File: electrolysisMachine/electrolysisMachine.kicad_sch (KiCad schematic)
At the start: 1 part

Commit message: started work on shcematic
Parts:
- added C?: 100n, Capacitor_SMD:C_0805_2012Metric_Pad1.18x1.45mm_HandSolder, symbol 000_Capacitor_FIlm_Immo:cap_film_0805
- added R?: 260r, Resistor_SMD:R_0805_2012Metric_Pad1.20x1.40mm_HandSolder, symbol 000_Resistors_Immo:Resistor_0805
- added SW?: Power, symbol Switch:SW_SPST
- added U?: LM317_SOT-223, Package_TO_SOT_THT:TO-220-3_Vertical, symbol Regulator_Linear:LM317_SOT-223
- added U?: LM317_TO-220, Package_SO:SOIC-8_3.9x4.9mm_P1.27mm, symbol Regulator_Linear:LM317_TO-220
- added Vtrim: 5k, Potentiometer_THT:Potentiometer_Alps_RK09K_Single_Vertical, symbol Device:R_Potentiometer_Trim
- J?: value XT60_connector_DC_60A_male -> XT60_60A_m
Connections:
- net 30V_BUS: now also C?.1, SW?.2 (B), U?.3 (VI), U?.3 (VI); no longer J?.2 (V+)
- net GNDPWR: now also C?.2, Vtrim.1
- new net: R?.2, U?.1 (ADJ), U?.1 (ADJ), Vtrim.2, Vtrim.3
- new net: J?.2 (V+), SW?.1 (A)
- new net V_ANODE: R?.1, U?.2 (VO), U?.2 (VO)
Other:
- note added: "Or use charge Pump?"

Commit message: nhj
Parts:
- added C? (x2): 1u, Capacitor_SMD:CP_Elec_6.3x5.9, symbol 000_Capacitor_Electrolytic_Immo:22u
- added C?: 100n, Capacitor_SMD:C_0805_2012Metric_Pad1.18x1.45mm_HandSolder, symbol 000_Capacitor_FIlm_Immo:cap_film_0805
- added D?: LED_0805_smd, Diode_SMD:D_0805_2012Metric_Pad1.15x1.40mm_HandSolder, symbol 000_Diodes_Immo:LED_0805_smd
- added R?: 260r, Resistor_SMD:R_0805_2012Metric_Pad1.20x1.40mm_HandSolder, symbol 000_Resistors_Immo:Resistor_0805
- added U?: L7805, Package_TO_SOT_THT:TO-220F-3_Horizontal_TabDown, symbol Regulator_Linear:L7805
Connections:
- net GNDPWR: now also C?.2, C?.2, C?.2, R?.2, U?.2 (GND)
- net V_ANODE: now also C?.1, C?.1, U?.1 (IN)
- new net: D?.1 (K), R?.1
- new net 5V_BUS: C?.1, D?.2 (A), U?.3 (OUT)

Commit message: Schematic Layout Continued
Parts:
- added J?: Anode/Cathode, symbol 000_Connectors_Immo:XT60_connector_DC_30A_female
- added Q?: PN2222A, Package_TO_SOT_SMD:SOT-223-3_TabPin2, symbol Transistor_BJT:PN2222A
- added R?: 1k, Resistor_SMD:R_0805_2012Metric_Pad1.20x1.40mm_HandSolder, symbol 000_Resistors_Immo:Resistor_0805
- added SW?: SW_SPST, symbol Switch:SW_SPST
- added TP?: A_meter, symbol Connector:TestPoint_2Pole
- added TP?: V_meter, symbol Connector:TestPoint_2Pole
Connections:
- net GNDPWR: now also R?.2, TP?.1
- net V_ANODE: now also J?.2 (V+), SW?.1 (A), TP?.2
- new net: Q?.1 (E), R?.1
- new net: Q?.3 (C), TP?.1
- new net: J?.1 (V-), SW?.2 (B), TP?.2

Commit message: schem
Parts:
- added C?: cap_film_0805, Capacitor_SMD:C_0805_2012Metric_Pad1.18x1.45mm_HandSolder, symbol 000_Capacitor_FIlm_Immo:cap_film_0805
- added D?: LED_ORANGE, Diode_SMD:D_0805_2012Metric_Pad1.15x1.40mm_HandSolder, symbol 000_Diodes_Immo:LED_0805_smd
- added Q?: 2N3906, Package_TO_SOT_THT:TO-92_Inline, symbol Transistor_BJT:2N3906
- added R: 1k2, Resistor_SMD:R_0805_2012Metric_Pad1.20x1.40mm_HandSolder, symbol 000_Resistors_Immo:Resistor_0805
- added R? (x2): 12k, Resistor_SMD:R_0805_2012Metric_Pad1.20x1.40mm_HandSolder, symbol 000_Resistors_Immo:Resistor_0805
- added R?: 2k9, Resistor_SMD:R_0805_2012Metric_Pad1.20x1.40mm_HandSolder, symbol 000_Resistors_Immo:Resistor_0805
- added R? (x3): 15k, Resistor_SMD:R_0805_2012Metric_Pad1.20x1.40mm_HandSolder, symbol 000_Resistors_Immo:Resistor_0805
- added R?: 2k2, Resistor_SMD:R_0805_2012Metric_Pad1.20x1.40mm_HandSolder, symbol 000_Resistors_Immo:Resistor_0805
- added RV?: Current, Potentiometer_THT:Potentiometer_Alpha_RD901F-40-00D_Single_Vertical, symbol Device:R_Potentiometer
- added U? (x5): LM324, symbol Amplifier_Operational:LM324
- D?: value LED_0805_smd -> LED_BLUE
- SW?: value SW_SPST -> TestLoad
- renumbered Vtrim to Voltage
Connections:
- net 5V_BUS: now also C?.1, R?.1, R?.2, R?.2, U?.12 (+), U?.4 (V+)
- net GNDPWR: now also C?.2, R.1, R?.1, R?.2, RV?.1, U?.11 (V-)
- net at Q?.1 (E), R?.1: now also U?.2 (-)
- net at Q?.2 (B): now also U?.1
- new net: U?.13 (-), U?.14
- new net: RV?.2, U?.3 (+)
- new net: R?.1, R?.2, U?.5 (+)
- new net: D?.1 (K), R.2
- new net: R?.1, R?.1, U?.7
- new net: Q?.2 (B), R?.2
- new net: R?.1, R?.2, U?.9 (-)
- new net: D?.2 (A), R?.2, U?.8
- new net: Q?.1 (E), R?.1
- new net: Q?.3 (C), RV?.3
- new net TRIGGER: U?.10 (+), U?.6 (-)
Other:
- note added: "Transistor Orientation Unclear"
- moved on the sheet: C?, D?, J?, Q?, R?, SW?, TP?, U?, Voltage

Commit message: 6y7iy
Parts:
- removed C?: cap_film_0805, Capacitor_SMD:C_0805_2012Metric_Pad1.18x1.45mm_HandSolder, symbol 000_Capacitor_FIlm_Immo:cap_film_0805
- added C?: cap_film_0805, Capacitor_SMD:C_0805_2012Metric_Pad1.18x1.45mm_HandSolder, symbol 000_Capacitor_Film_Immo:cap_film_0805
- C? (x2): symbol 000_Capacitor_FIlm_Immo:cap_film_0805 -> 000_Capacitor_Film_Immo:cap_film_0805
- J?: symbol 000_Connectors_Immo:XT60_connector_DC_30A_female -> 000_Connectors_Immo:XT30_connector_DC_30A_female
- J?: symbol 000_Connectors_Immo:XT60_connector_DC_60A_male -> 000_Connectors_Immo:XT60_60A_male
- PT?: renamed from Voltage; footprint Potentiometer_THT:Potentiometer_Alps_RK09K_Single_Vertical -> Potentiometer_THT:Potentiometer_Alpha_RD901F-40-00D_Single_Vertical_CircularHoles; symbol Device:R_Potentiometer_Trim -> 000_Resistors_Immo:Potentiometer; Control (none) -> Current
- PT?: renamed from RV?; footprint Potentiometer_THT:Potentiometer_Alpha_RD901F-40-00D_Single_Vertical -> Potentiometer_THT:Potentiometer_Alpha_RD901F-40-00D_Single_Vertical_CircularHoles; symbol Device:R_Potentiometer -> 000_Resistors_Immo:Potentiometer; Control (none) -> Current
- Q?: footprint Package_TO_SOT_SMD:SOT-223-3_TabPin2 -> Package_TO_SOT_THT:TO-92_Inline
- U?: footprint Package_TO_SOT_THT:TO-220-3_Vertical -> Package_TO_SOT_SMD:SOT-223-3_TabPin2
- U?: footprint Package_SO:SOIC-8_3.9x4.9mm_P1.27mm -> Package_TO_SOT_THT:TO-220-3_Vertical
- gave numbers to parts that had none: 1
- renumbered R to R?
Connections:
- net 5V_BUS: now also R?.1, R?.1, R?.2, C?.1; no longer R?.1, R?.2, R?.2
- net GNDPWR: now also R?.1, R?.1, R?.1, R?.2, R?.2, C?.2; no longer R?.1, R?.1, R?.2, R?.2, R?.2
- net V_ANODE: now also R?.2; no longer R?.1
- net at PT?.2, PT?.3, U?.1 (ADJ)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: now also R?.1; no longer R?.2
- net at Q?.1 (E), U?.2 (-): now also R?.2; no longer R?.1
- net at D?.1 (K): now also R?.1; no longer R?.2
- net at Q?.2 (B): now also R?.1; no longer R?.2
- net at D?.1 (K): now also R?.2; no longer R?.1
- net at D?.2 (A), U?.8: now also R?.1; no longer R?.2
- net at Q?.1 (E): now also R?.2; no longer R?.1
- new net: R?.1, R?.2, U?.5 (+)
- new net: R?.2, R?.2, U?.7
- new net: R?.1, R?.2, U?.9 (-)
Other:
- moved on the sheet: R?

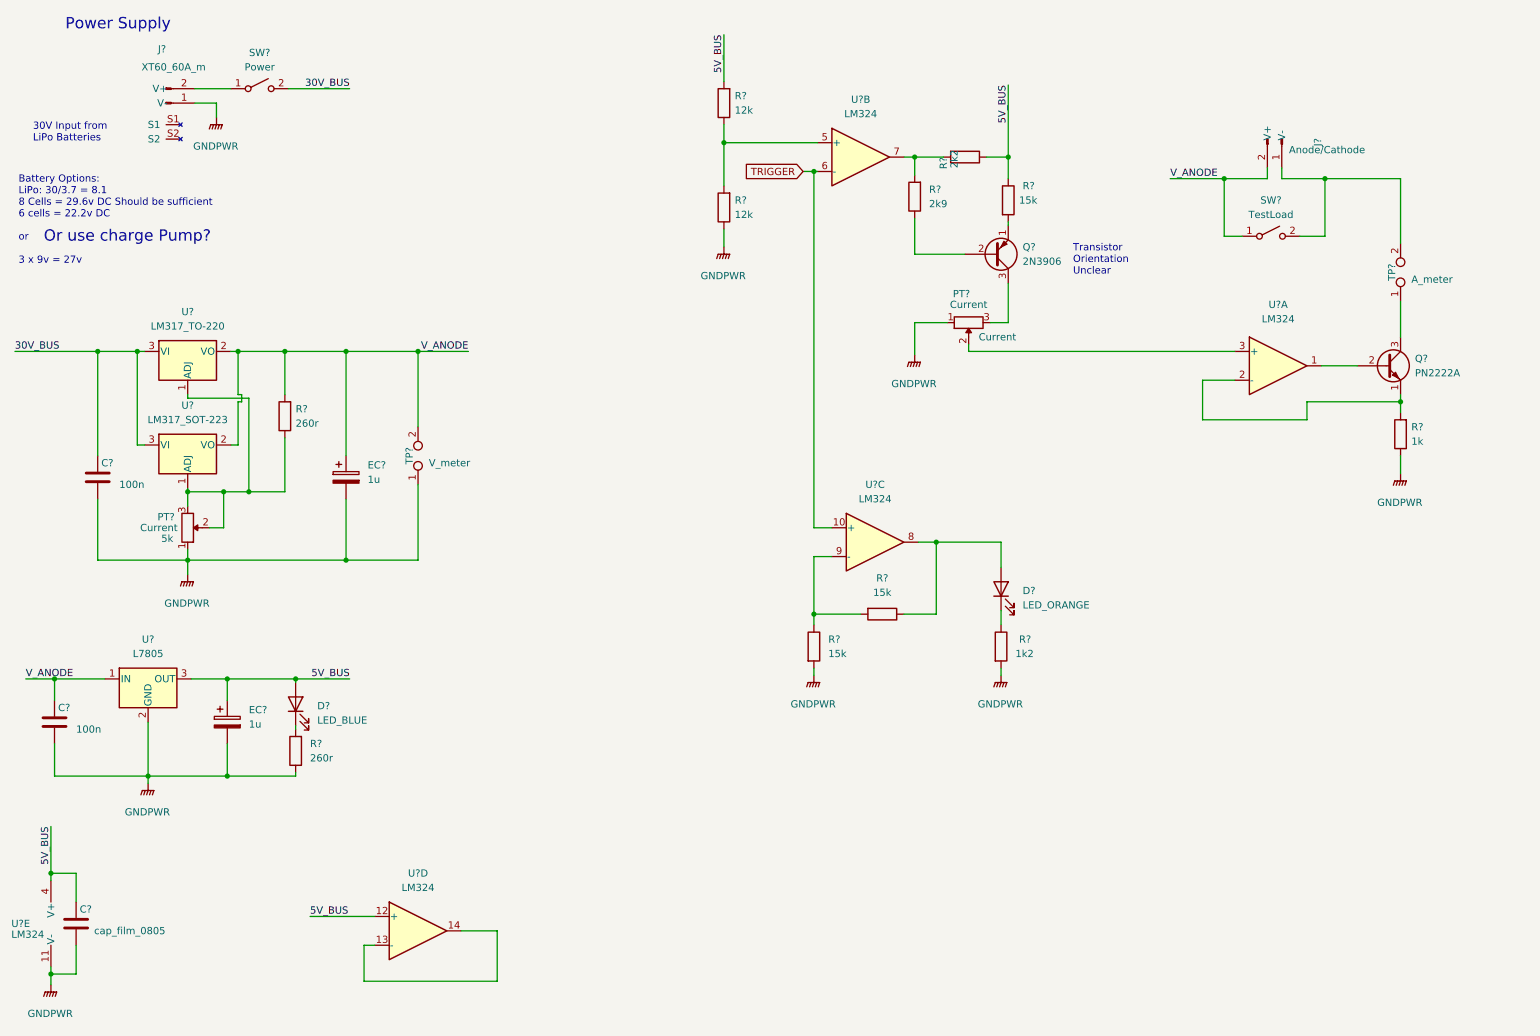
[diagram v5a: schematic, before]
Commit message: Organising schem and added hirarchical sheets
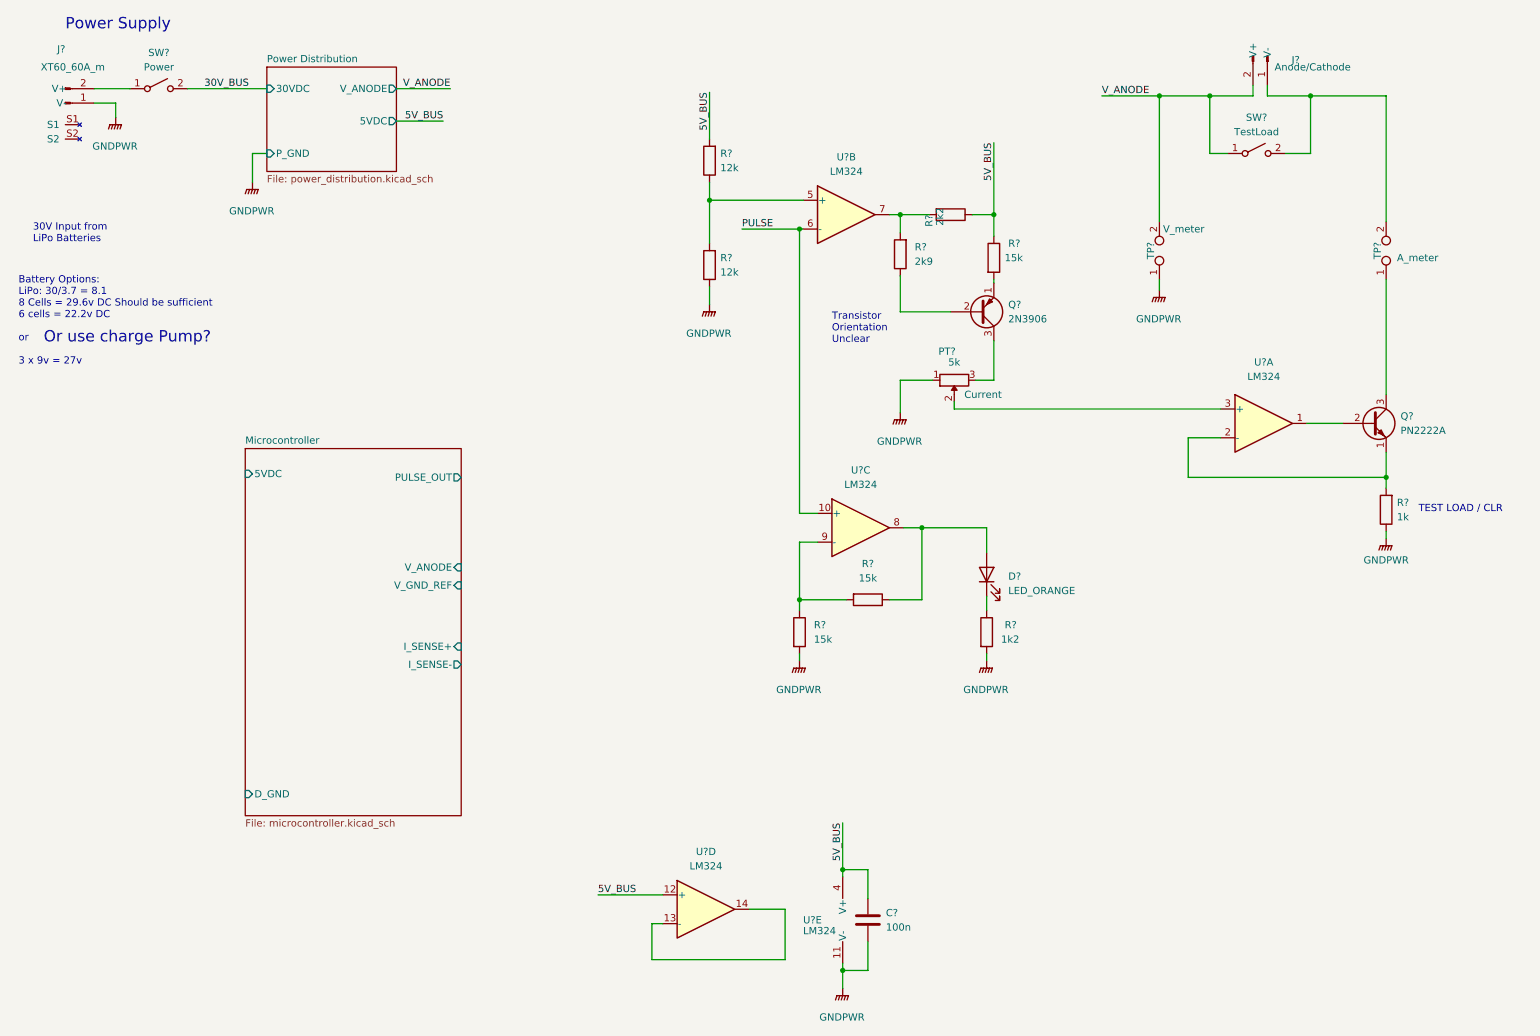
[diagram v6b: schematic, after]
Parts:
- removed C? (x2): 100n, Capacitor_SMD:C_0805_2012Metric_Pad1.18x1.45mm_HandSolder, symbol 000_Capacitor_Film_Immo:cap_film_0805
- removed D?: LED_BLUE, Diode_SMD:D_0805_2012Metric_Pad1.15x1.40mm_HandSolder, symbol 000_Diodes_Immo:LED_0805_smd
- removed EC? (x2): 1u, Capacitor_SMD:CP_Elec_6.3x5.9, symbol 000_Capacitor_Electrolytic_Immo:22u
- removed PT?: 5k, Potentiometer_THT:Potentiometer_Alpha_RD901F-40-00D_Single_Vertical_CircularHoles, symbol 000_Resistors_Immo:Potentiometer
- removed R? (x2): 260r, Resistor_SMD:R_0805_2012Metric_Pad1.20x1.40mm_HandSolder, symbol 000_Resistors_Immo:Resistor_0805
- removed TP?: V_meter, symbol Connector:TestPoint_2Pole
- removed U?: LM317_SOT-223, Package_TO_SOT_SMD:SOT-223-3_TabPin2, symbol Regulator_Linear:LM317_SOT-223
- removed U?: LM317_TO-220, Package_TO_SOT_THT:TO-220-3_Vertical, symbol Regulator_Linear:LM317_TO-220
- removed U?: L7805, Package_TO_SOT_THT:TO-220F-3_Horizontal_TabDown, symbol Regulator_Linear:L7805
- added TP?: V_meter, symbol Connector:TestPoint_2Pole
- C?: value cap_film_0805 -> 100n
- PT?: value Current -> 5k
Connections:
- net GNDPWR: now also TP?.1
- net V_ANODE: now also TP?.2
- net TRIGGER renamed PULSE
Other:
- added sheet Microcontroller (microcontroller.kicad_sch)
- added sheet Power Distribution (power_distribution.kicad_sch)
- note added: "TEST LOAD / CLR"
- moved on the sheet: C?, D?, J?, PT?, Q?, R?, SW?, TP?, U?A, U?B, U?C, U?D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
